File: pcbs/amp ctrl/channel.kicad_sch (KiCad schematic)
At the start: 98 parts, among them J11 Conn_01x02, J6 Conn_02x02, J8 Conn_02x10_Odd_Even, J9 Conn_02x02, J92 Conn_01x02, Q1 MMBT3904, Q2 MMBT3906, Q3 MMBT3904, Q36 MMBT3904, Q37 2N7002, Q4 MMBT3906, U1 INA821/819, U2 OPA37, U3 ADA4004-1, U7 TLVH431, U73 TBD, U9 TLVH431

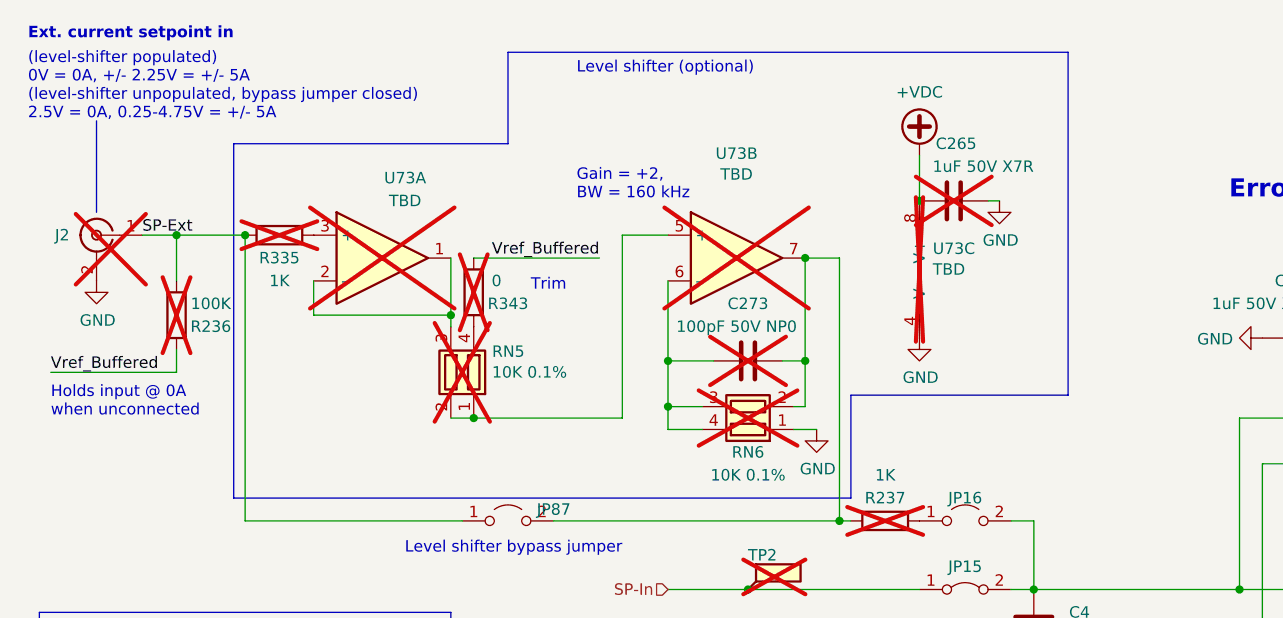
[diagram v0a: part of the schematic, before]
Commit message: Backplane comms updates, manufacturing renaming
Removed misspelled "maunfacturing" folder, fixed gitignore rule to remove manufacturing folders within individual PCB folders too
Changed SCKI/SCKO terminology to SCK, SCK_LB (loopback) for clarity
Added ADC_CS loopback signal between amp ctrl board & backplane for better fast-clock timing (#38)
Backplane: changed LVDS FPGA outputs to single-ended FPGA outputs to gain more I/O pins, added external LVDS transceivers (#38)
Backplane: replaced global clock & ~LDAC buffers with a separate FPGA pin for each amp ctrl board (#38)
Backplane: removed +2.5V power supply and level translations, no longer needed without FPGA I/O pins using LVDS_25 I/O configuration
Backplane: replaced +VDC-input resistor with solder jumper (on by default)
Backplane: changed field names (Part Number to MPN) to match Aisler's naming convention for automatic recognition
Amp ctrl: fixed optional level-shifter circuit on each channel for voltage inputs (#9) schematic & channel-1 layout
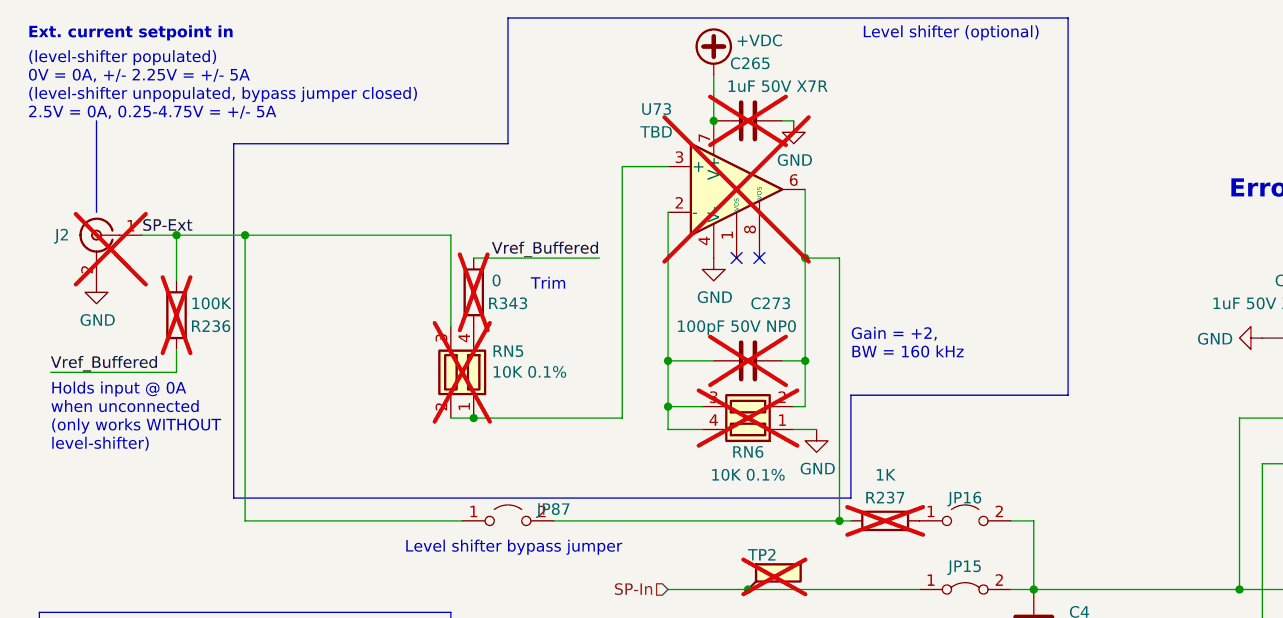
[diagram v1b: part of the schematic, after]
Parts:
- removed R335: 1K, Resistor_SMD:R_0805_2012Metric, symbol Device:R
- removed unit 2 of U73
- removed unit 3 of U73
- J2, J3, J5: value ~ -> (none)
- U73: symbol amp-ctrl-rescue:Opamp_Dual_Generic-Device -> Amplifier_Operational:OP07
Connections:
- net +VDC: now also U73.7 (V+)
- net GND: now also U73.4 (V-)
- net SP-Ext: now also RN5.3 (R2.2)
- net at C273.1, JP87.2 (B), R237.1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: now also U73.6
- net at RN5.1 (R1.1), RN5.2 (R2.1): now also U73.3 (+)
- net at C273.2, RN6.3 (R2.2), RN6.4 (R1.2): now also U73.2 (-)
- now unconnected: U73.1
- no-connect marks 0 -> 2
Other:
- note added: "Holds input @ 0A when unconnected (only works WITHOUT level-shifter)"
- note removed: "Holds input @ 0A when unconnected"
- moved on the sheet: C265
